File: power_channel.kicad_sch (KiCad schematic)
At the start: 60 parts, among them Q1 IRF100B201, Q2 IRF100B201, Q3 IRF100B201, Q4 IRF100B201, U1 IR2184, U2 IR2184, U3 INA240A1D, U4 LM393, U5 74HC74

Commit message: Schematic complete: all sheets wired, ERC clean, netlist verified, cap ratings set
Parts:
- C1, C16, C18, C4: Voltage (none) -> 25V
- C11, C12, C13, C14, C15, C17, C2, C20, C21, C22, C23, C3, C5, C6, C7, C8: Voltage (none) -> 100V
- C19: Voltage (none) -> 50V
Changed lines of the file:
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@@
 			)
 		)
+		(property "Voltage" "100V"
+			(at 161.29 43.18 0)
+			(hide yes)
+			(show_name no)
+			(do_not_autoplace no)
+			(effects
+				(font
+					(size 1.27 1.27)
+				)
+			)
+		)
 		(pin "1"
 		)
@@
 			)
 		)
+		(property "Voltage" "100V"
+			(at 114.3 157.48 0)
+			(hide yes)
+			(show_name no)
+			(do_not_autoplace no)
+			(effects
+				(font
+					(size 1.27 1.27)
+				)
+			)
+		)
 		(pin "1"
 		)
@@
 			)
 		)
+		(property "Voltage" "100V"
+			(at 173.99 157.48 0)
+			(hide yes)
+			(show_name no)
+			(do_not_autoplace no)
+			(effects
+				(font
+					(size 1.27 1.27)
+				)
+			)
+		)
 		(pin "2"
 		)
@@
 			)
 		)
+		(property "Voltage" "100V"
+			(at 69.85 49.53 90)
+			(hide yes)
+			(show_name no)
+			(do_not_autoplace no)
+			(effects
+				(font
+					(size 1.27 1.27)
+				)
+			)
+		)
 		(pin "1"
 		)
@@
 			)
 		)
+		(property "Voltage" "100V"
+			(at 66.04 157.48 0)
+			(hide yes)
+			(show_name no)
+			(do_not_autoplace no)
+			(effects
+				(font
+					(size 1.27 1.27)
+				)
+			)
+		)
 		(pin "2"
 		)
@@
 			)
 		)
+		(property "Voltage" "50V"
+			(at 39.37 60.96 0)
+			(hide yes)
+			(show_name no)
+			(do_not_autoplace no)
+			(effects
+				(font
+					(size 1.27 1.27)
+				)
+			)
+		)
 		(pin "1"
 		)
@@
 			)
 		)
+		(property "Voltage" "100V"
+			(at 77.47 157.48 0)
+			(hide yes)
+			(show_name no)
+			(do_not_autoplace no)
+			(effects
+				(font
+					(size 1.27 1.27)
+				)
+			)
+		)
 		(pin "2"
 		)
@@
 			)
 		)
+		(property "Voltage" "100V"
+			(at 339.09 31.75 0)
+			(hide yes)
+			(show_name no)
+			(do_not_autoplace no)
+			(effects
+				(font
+					(size 1.27 1.27)
+				)
+			)
+		)
 		(pin "1"
 		)
@@
 			)
 		)
+		(property "Voltage" "100V"
+			(at 210.82 157.48 0)
+			(hide yes)
+			(show_name no)
+			(do_not_autoplace no)
+			(effects
+				(font
+					(size 1.27 1.27)
+				)
+			)
+		)
 		(pin "1"
 		)
@@
 			)
 		)
+		(property "Voltage" "25V"
+			(at 375.92 99.06 0)
+			(hide yes)
+			(show_name no)
+			(do_not_autoplace no)
+			(effects
+				(font
+					(size 1.27 1.27)
+				)
+			)
+		)
 		(pin "1"
 		)
@@
 			)
 		)
+		(property "Voltage" "100V"
+			(at 100.33 157.48 0)
+			(hide yes)
+			(show_name no)
+			(do_not_autoplace no)
+			(effects
+				(font
+					(size 1.27 1.27)
+				)
+			)
+		)
 		(pin "2"
 		)
@@
 			)
 		)
+		(property "Voltage" "25V"
+			(at 377.19 43.18 0)
+			(hide yes)
+			(show_name no)
+			(do_not_autoplace no)
+			(effects
+				(font
+					(size 1.27 1.27)
+				)
+			)
+		)
 		(pin "1"
 		)
@@
 			)
 		)
+		(property "Voltage" "25V"
+			(at 328.93 110.49 0)
+			(hide yes)
+			(show_name no)
+			(do_not_autoplace no)
+			(effects
+				(font
+					(size 1.27 1.27)
+				)
+			)
+		)
 		(pin "1"
 		)
@@
 			)
 		)
+		(property "Voltage" "100V"
+			(at 185.42 157.48 0)
+			(hide yes)
+			(show_name no)
+			(do_not_autoplace no)
+			(effects
+				(font
+					(size 1.27 1.27)
+				)
+			)
+		)
 		(pin "2"
 		)
@@
 			)
 		)
+		(property "Voltage" "100V"
+			(at 367.03 99.06 0)
+			(hide yes)
+			(show_name no)
+			(do_not_autoplace no)
+			(effects
+				(font
+					(size 1.27 1.27)
+				)
+			)
+		)
 		(pin "1"
 		)
@@
 			)
 		)
+		(property "Voltage" "25V"
+			(at 330.2 31.75 0)
+			(hide yes)
+			(show_name no)
+			(do_not_autoplace no)
+			(effects
+				(font
+					(size 1.27 1.27)
+				)
+			)
+		)
 		(pin "1"
 		)
@@
 			)
 		)
+		(property "Voltage" "100V"
+			(at 298.45 35.56 90)
+			(hide yes)
+			(show_name no)
+			(do_not_autoplace no)
+			(effects
+				(font
+					(size 1.27 1.27)
+				)
+			)
+		)
 		(pin "1"
 		)
@@
 			)
 		)
+		(property "Voltage" "100V"
+			(at 196.85 157.48 0)
+			(hide yes)
+			(show_name no)
+			(do_not_autoplace no)
+			(effects
+				(font
+					(size 1.27 1.27)
+				)
+			)
+		)
 		(pin "2"
 		)
@@
 			)
 		)
+		(property "Voltage" "100V"
+			(at 229.87 73.66 0)
+			(hide yes)
+			(show_name no)
+			(do_not_autoplace no)
+			(effects
+				(font
+					(size 1.27 1.27)
+				)
+			)
+		)
 		(pin "1"
 		)
@@
 			)
 		)
+		(property "Voltage" "100V"
+			(at 162.56 157.48 0)
+			(hide yes)
+			(show_name no)
+			(do_not_autoplace no)
+			(effects
+				(font
+					(size 1.27 1.27)
+				)
+			)
+		)
 		(pin "2"
 		)
@@
 			(at 88.9 157.48 0)
 			(hide yes)
+			(show_name no)
+			(do_not_autoplace no)
+			(effects
+				(font
+					(size 1.27 1.27)
+				)
+			)
+		)
+		(property "Voltage" "100V"
+			(at 88.9 157.48 0)
+			(hide yes)

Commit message: Adversarial review fixes: set-dominant latch, MCU enable, 3V3 hold-up, sense chain, 16-way connector
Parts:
- added C24, C25, C26: 100nF, Capacitor_SMD:C_0805_2012Metric_Pad1.18x1.45mm_HandSolder, symbol Device:C
- added C27: 4.7nF, Capacitor_SMD:C_0805_2012Metric_Pad1.18x1.45mm_HandSolder, symbol Device:C
- added R24, R25: 10k, Resistor_SMD:R_0805_2012Metric_Pad1.20x1.40mm_HandSolder, symbol Device:R
- added R26: 3.3k, Resistor_SMD:R_0805_2012Metric_Pad1.20x1.40mm_HandSolder, symbol Device:R
- added R27: 1k, Resistor_SMD:R_0805_2012Metric_Pad1.20x1.40mm_HandSolder, symbol Device:R
- added U6: 74HCT00, Package_SO:SOIC-14_3.9x8.7mm_P1.27mm, symbol 74xx:74HCT00
- R11: value 1m -> 0.5m; MPN (none) -> WSK2512L5000FEA
- R15: value 24k -> 43k
- U3: value INA240A1D -> INA240A2D; symbol Amplifier_Current:INA240A1D -> Amplifier_Current:INA240A2D
- U4: value LM393 -> LM2903B; MPN LM393DR -> LM2903BDR
- U5: value 74HC74 -> 74HCT74; symbol 74xx:74HC74 -> 74xx:74HCT74
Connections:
- net +5V: now also C24.1, U6.14 (VCC)
- net FAULT_N: now also U6.5
- net GND: now also C24.2, C25.1, C26.1, C27.2, R24.2, R25.2, U6.7 (GND)
- net ISNS: now also R27.1; no longer U4.2 (-), U4.5 (+)
- net PWM_A: now also R24.1
- net PWM_B: now also R25.1
- net RESET: now also U6.1, U6.2; no longer U5.1 (~{R})
- net SD: now also R26.2; no longer U5.6 (~{Q})
- net VTH_HI: now also C25.2
- net VTH_LO: now also C26.2
- net FAULT: no longer names the net of U5.5 (Q)
- new net EN: U6.10
- new net ISNS_F: C27.1, R27.2, U4.2 (-), U4.5 (+)
- new net OK: R26.1, U6.11
- new net RESET_EFF: U5.1 (~{R}), U6.6
- new net RESET_N: U6.3, U6.4
- new net SD_N: U6.12, U6.13, U6.8
- new net SD_Q: U5.6 (~{Q}), U6.9
- no-connect marks 2 -> 3
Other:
- moved on the sheet: C22, C23, R18, U5A, U5B, U5C

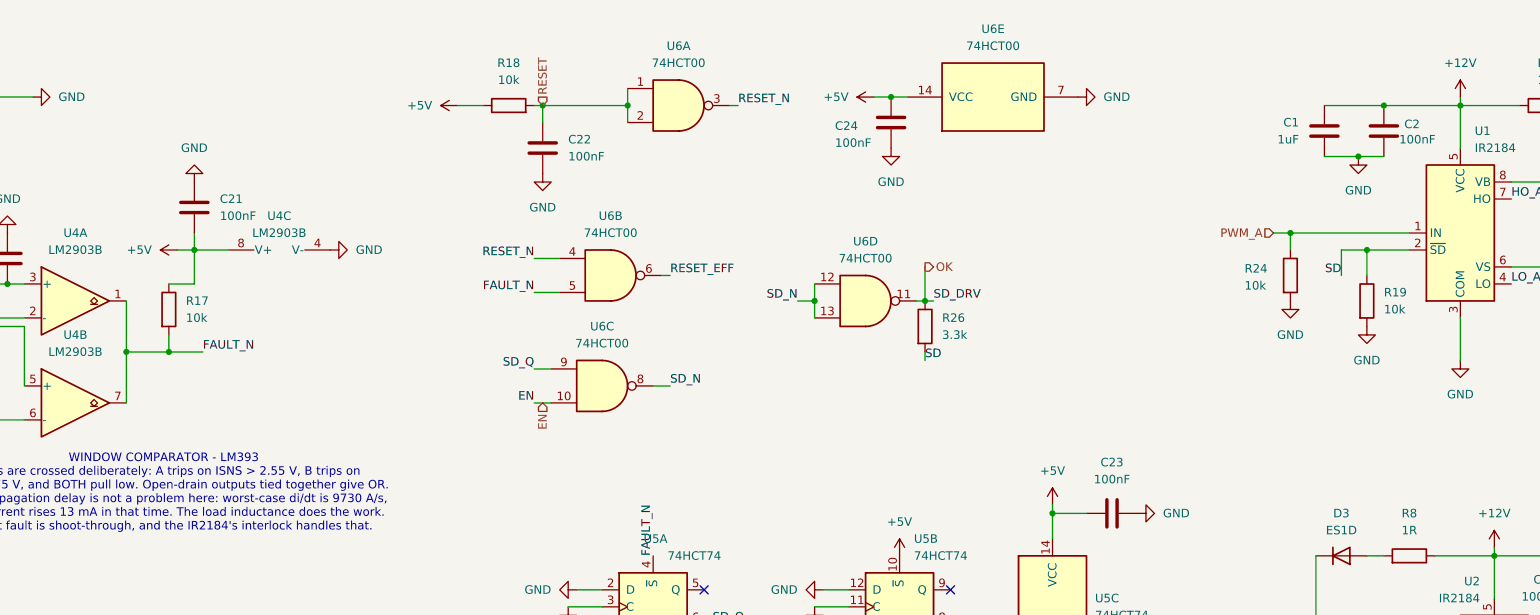
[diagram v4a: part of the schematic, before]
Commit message: Delta review fixes: POR timing, comparator supply, trip point, SD divider, Schmitt gate
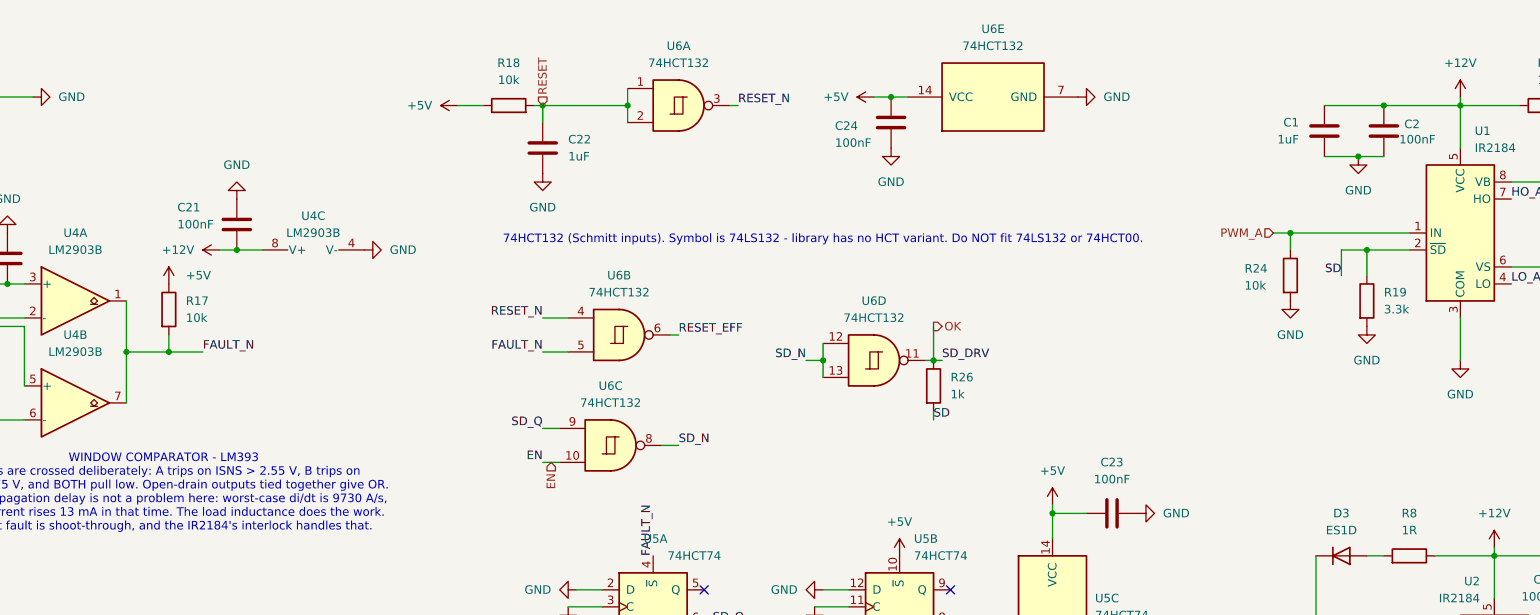
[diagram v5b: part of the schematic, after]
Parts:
- C22: value 100nF -> 1uF; Voltage 100V -> 25V
- R19: value 10k -> 3.3k
- R26: value 3.3k -> 1k
- U6: value 74HCT00 -> 74HCT132; symbol 74xx:74HCT00 -> 74xx:74LS132; MPN (none) -> 74HCT132D,653
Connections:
- net +12V: now also C21.2, U4.8 (V+)
- net +5V: no longer C21.2, U4.8 (V+)
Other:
- note added: "74HCT132 (Schmitt inputs). Symbol is 74LS132 - library has no HCT variant. Do NOT fit 74LS132 or 74HCT00."
- moved on the sheet: C21, R26, U4C

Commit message: Interleave corrected 180->90 deg; U5 D pin to fail-safe; review addendum 2
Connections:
- net +5V: now also U5.2 (D)
- net GND: no longer U5.2 (D)
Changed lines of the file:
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@@
 		(comment 3 "PROVISIONAL — coil L, k and R are unmeasured. See assumption register on this sheet.")
 		(comment 4 "Design record: docs/09_design_sheet_rev0.md · review: docs/16_adversarial_review.md")
-		(comment 5 "MODULATION: unipolar 3-level PWM (leg A = D, leg B = 1-D). Channels interleaved 180 deg. The 180 deg interleave is required, not optional - see A14.")
+		(comment 5 "MODULATION: unipolar 3-level PWM (leg A = D, leg B = 1-D). Channels interleaved 90 deg. The 90 deg interleave is required, not optional - see A14.")
 	)
 	(text "ALL BUS CAPS ≥100 V, X7R · BULK ELECTROLYTICS ON BUS SHEET"
@@
 	)
 	(symbol
+		(lib_id "power:+5V")
+		(at 218.44 100.33 0)
+		(unit 1)
+		(body_style 1)
+		(exclude_from_sim no)
+		(in_bom yes)
+		(on_board yes)
+		(in_pos_files yes)
+		(dnp no)
+		(fields_autoplaced yes)
+		(property "Reference" "#PWR0241"
+			(at 218.44 104.14 0)
+			(hide yes)
+			(show_name no)
+			(do_not_autoplace no)
+			(effects
+				(font
+					(size 1.27 1.27)
+				)
+			)
+		)
+		(property "Value" "+5V"
+			(at 218.44 95.25 0)
+			(show_name no)
+			(do_not_autoplace no)
+			(effects
+				(font
+					(size 1.27 1.27)
+				)
+			)
+		)
+		(property "Footprint" ""
+			(at 218.44 100.33 0)
+			(hide yes)
+			(show_name no)
+			(do_not_autoplace no)
+			(effects
+				(font
+					(size 1.27 1.27)
+				)
+			)
+		)
+		(property "Datasheet" ""
+			(at 218.44 100.33 0)
+			(hide yes)
+			(show_name no)
+			(do_not_autoplace no)
+			(effects
+				(font
+					(size 1.27 1.27)
+				)
+			)
+		)
+		(property "Description" "Power symbol creates a global label with name \"+5V\""
+			(at 218.44 100.33 0)
+			(hide yes)
+			(show_name no)
+			(do_not_autoplace no)
+			(effects
+				(font
+					(size 1.27 1.27)
+				)
+			)
+		)
+		(pin "1"
+		)
+		(instances
+			(project "final_lev"
+				(path "/0a40c0f2-6b4c-4590-a920-c8cc820982d1/4e830c1e-538f-4dbb-bf01-d2466ce385dd"
+					(reference "#PWR0242")
+					(unit 1)
+				)
+				(path "/0a40c0f2-6b4c-4590-a920-c8cc820982d1/caa4a5a4-3670-4710-8301-952cca866c48"
+					(reference "#PWR0241")
+					(unit 1)
+				)
+			)
+		)
+	)
+	(symbol
 		(lib_id "Comparator:LM393")
 		(at 143.51 72.39 0)
@@
 					(unit 1)
 				)
-			)
-		)
-	)
-	(symbol
-		(lib_id "power:GND")
-		(at 218.44 100.33 270)
-		(unit 1)
-		(body_style 1)
-		(exclude_from_sim no)
-		(in_bom yes)
-		(on_board yes)
-		(in_pos_files yes)
-		(dnp no)
-		(fields_autoplaced yes)
-		(property "Reference" "#PWR021"
-			(at 212.09 100.33 0)
-			(hide yes)
-			(show_name no)
-			(do_not_autoplace no)
-			(effects
-				(font
-					(size 1.27 1.27)
-				)
-			)
-		)
-		(property "Value" "GND"
-			(at 214.63 100.3299 90)
-			(show_name no)
-			(do_not_autoplace no)
-			(effects
-				(font
-					(size 1.27 1.27)
-				)
-				(justify right)
-			)
-		)
-		(property "Footprint" ""
-			(at 218.44 100.33 0)
-			(hide yes)
-			(show_name no)
-			(do_not_autoplace no)
-			(effects
-				(font
-					(size 1.27 1.27)
-				)
-			)
-		)
-		(property "Datasheet" ""
-			(at 218.44 100.33 0)
-			(hide yes)
-			(show_name no)
-			(do_not_autoplace no)
-			(effects
-				(font
-					(size 1.27 1.27)
-				)
-			)
-		)
-		(property "Description" "Power symbol creates a global label with name \"GND\" , ground"
-			(at 218.44 100.33 0)
-			(hide yes)
-			(show_name no)
-			(do_not_autoplace no)
-			(effects
-				(font
-					(size 1.27 1.27)
-				)
-			)
-		)
-		(pin "1"
-		)
-		(instances
-			(project "final_lev"
-				(path "/0a40c0f2-6b4c-4590-a920-c8cc820982d1/4e830c1e-538f-4dbb-bf01-d2466ce385dd"
-					(reference "#PWR0329")
-					(unit 1)
-				)
-				(path "/0a40c0f2-6b4c-4590-a920-c8cc820982d1/caa4a5a4-3670-4710-8301-952cca866c48"
-					(reference "#PWR021")
-					(unit 1)
-				)

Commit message: Coil pours, test points, and a pad-rotation defect found by tooling
Board:

- 13 test points placed, grounds first so every signal point sits within 7.5 mm of its own ground return

- All four 30 A coil pours drawn on B.Cu, single polygons, 10.7-11.0 mm at the narrowest cut

- 34 vias transitioning the two A legs from the surface-mount shunts down to B.Cu, 15 at 2.0 A on CH1 and 19 at 1.58 A on CH2

- The B legs need no vias: every pad carrying their current is through-hole

Fixed:

- 20 footprints had pads that did not follow their body rotation, 5 of them off by 90 degrees, which turns a 1.175 x 1.450 mm pad across the part instead of along it. Repaired by Update Footprints from Library

- A12 corrected twice. The mounting holes are plated M3 pads on all four layers with no net, not the unplated holes I first reported

Tools:

- pour_check.py rasterises pour outlines at 0.05 mm; lay.py's bounding-box zone check was blind to polygons and missed a 6.5 mm band that needed 10.7

- lay.py gained pad-rotation and zone-priority checks, both regression tested against the broken versions
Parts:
- added TP201, TP203, TP205, TP207: TestPoint, TestPoint:TestPoint_Loop_D2.50mm_Drill1.0mm, symbol Connector:TestPoint
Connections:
- net FAULT_N: now also TP205.1
- net GND: now also TP207.1
- net ISNS: now also TP201.1
- net SD: now also TP203.1
